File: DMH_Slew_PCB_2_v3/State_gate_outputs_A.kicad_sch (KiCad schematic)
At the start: 26 parts, among them J4 TS_Jack_6.35mm_Sw, J5 TS_Jack_6.35mm_Sw, J51 Conn_01x08_PinHeader, Q5 BC548, Q6 BC548, U1 TL074

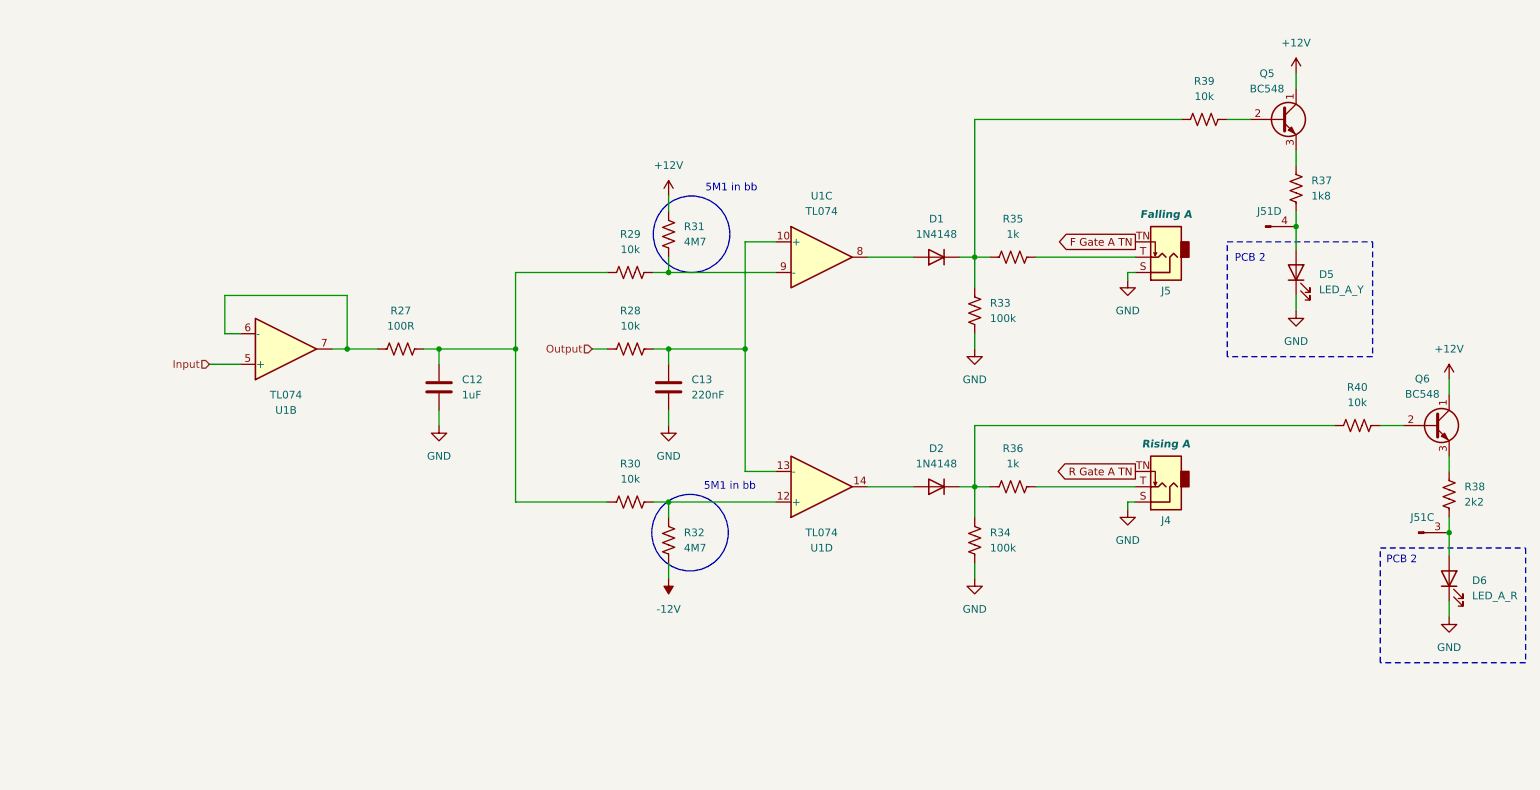
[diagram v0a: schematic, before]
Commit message: Relinked PCB1 and 2 with new v3 schematics
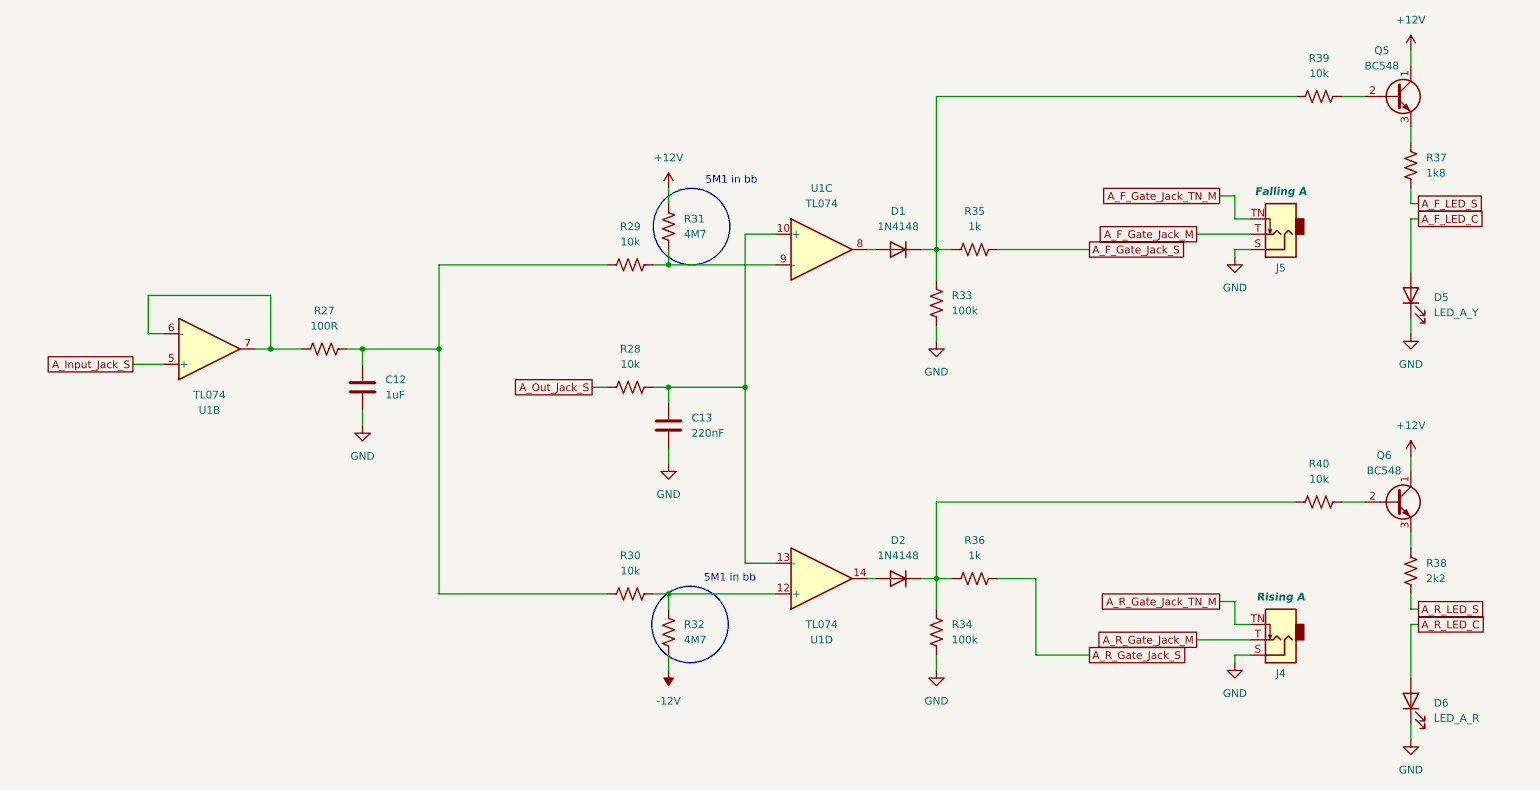
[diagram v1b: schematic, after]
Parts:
- removed J51: Conn_01x08_PinHeader, Connector_PinSocket_2.54mm:PinSocket_1x08_P2.54mm_Vertical, symbol SynthStuff:Conn_01x08_PinHeader
- Q5: footprint Package_TO_SOT_THT:TO-92L_Inline_Wide -> Package_TO_SOT_THT:TO-92_Inline
- U1: footprint Package_DIP:DIP-16_W7.62mm_Socket -> Package_DIP:DIP-14_W7.62mm_Socket
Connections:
- net A_R_LED_C: now reaches D6.2 (A)
- net A_R_LED_C: no longer R38.2
- net A_F_Gate_Jack_M: now reaches J5.T
- net A_F_Gate_Jack_M: no longer R35.1
- net A_F_LED_C: now reaches D5.2 (A)
- net A_F_LED_C: no longer R37.2
- net A_R_Gate_Jack_M: now reaches J4.T
- net A_R_Gate_Jack_M: no longer R36.1
- net F Gate A TN renamed A_F_Gate_Jack_TN_M
- net Input renamed A_Input_Jack_S
- net Output renamed A_Out_Jack_S
- net R Gate A TN renamed A_R_Gate_Jack_TN_M
- new net A_F_Gate_Jack_S: R35.1
- new net A_F_LED_S: R37.2
- new net A_R_Gate_Jack_S: R36.1
- new net A_R_LED_S: R38.2
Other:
- note removed: "PCB 2"
- moved on the sheet: C12, C13, D1, D2, D5, D6, J4, J5, Q5, Q6, R27, R28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

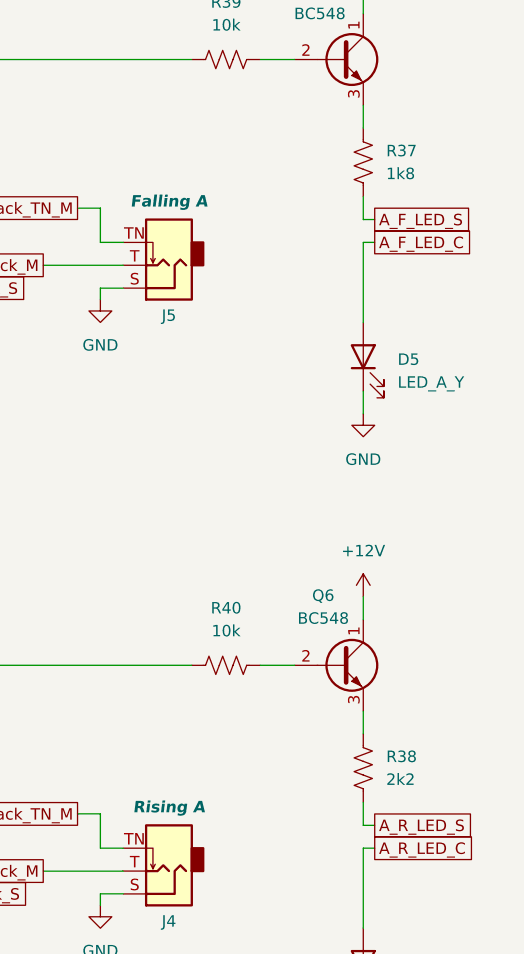
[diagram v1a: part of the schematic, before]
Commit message: Corrected PCB 2 switch positions
and Regenerated Gerbers
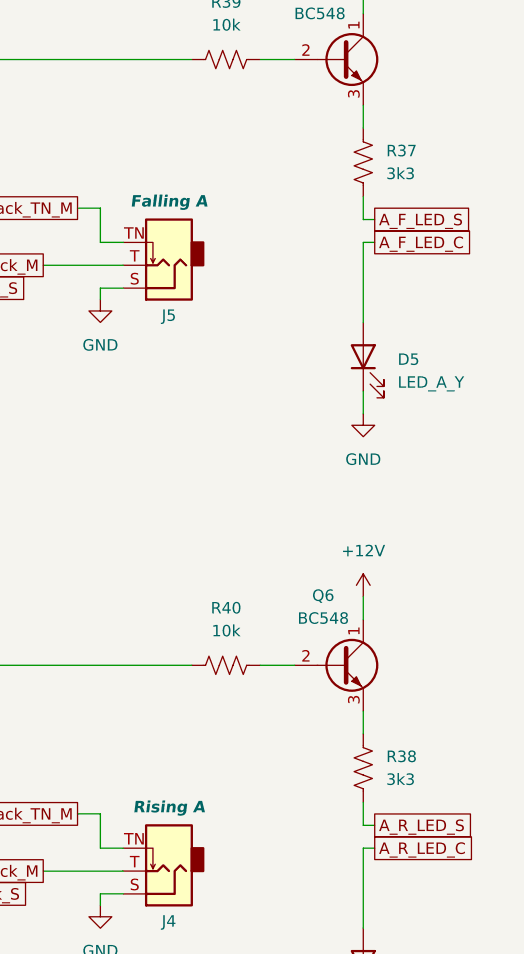
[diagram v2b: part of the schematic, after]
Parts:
- R37: value 1k8 -> 3k3
- R38: value 2k2 -> 3k3
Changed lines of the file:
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@@
 			)
 		)
-		(property "Value" "2k2"
+		(property "Value" "3k3"
 			(at 252.73 114.2999 0)
 			(effects
@@
 			)
 		)
-		(property "Value" "1k8"
+		(property "Value" "3k3"
 			(at 252.73 46.9899 0)
 			(effects

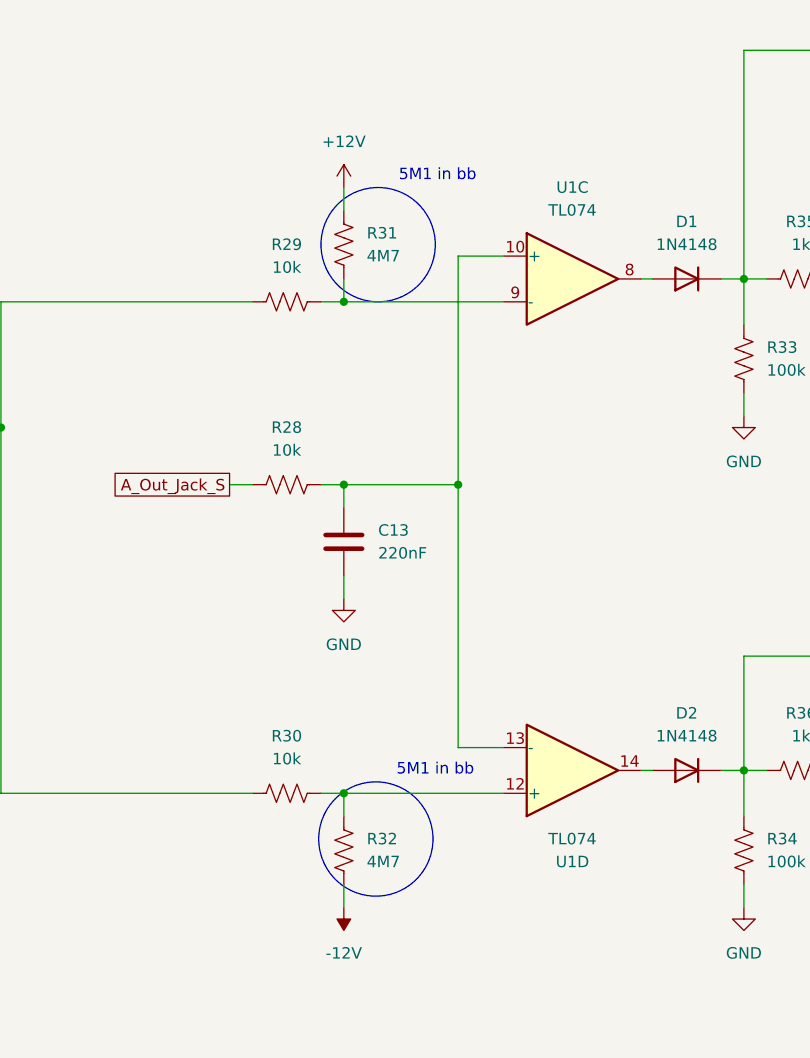
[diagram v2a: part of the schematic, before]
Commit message: Redesigned Main PCB
and regenerated Gerbers
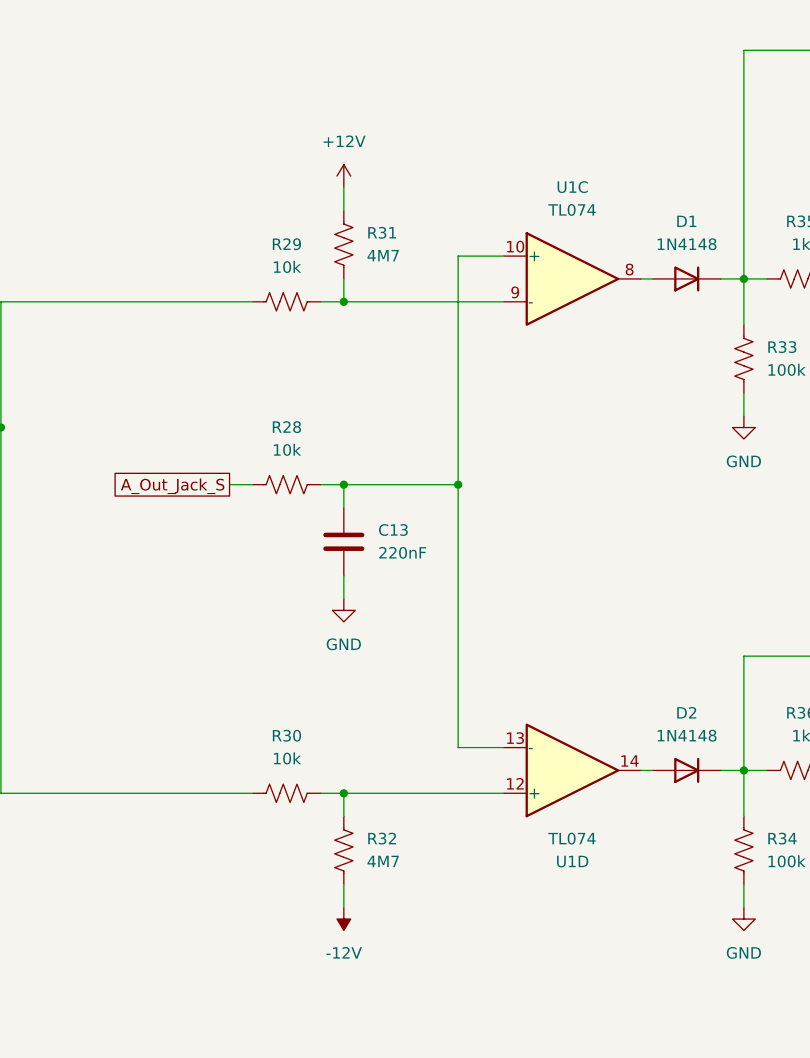
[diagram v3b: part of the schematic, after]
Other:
- note removed: "5M1 in bb"
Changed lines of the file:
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@@
 		(comment 1 "PCB for 5 cm Kosmo format synthesizer module")
-	)
-	(circle
-		(center 130.556 121.92)
-		(radius 6.35)
-		(stroke
-			(width 0)
-			(type default)
-		)
-		(fill
-			(type none)
-		)
-	)
-	(circle
-		(center 130.81 55.88)
-		(radius 6.35)
-		(stroke
-			(width 0)
-			(type default)
-		)
-		(fill
-			(type none)
-		)
-	)
-	(text "5M1 in bb"
-		(exclude_from_sim no)
-		(at 137.16 114.3 0)
-		(effects
-			(font
-				(size 1.27 1.27)
-			)
-		)
-	)
-	(text "5M1 in bb"
-		(exclude_from_sim no)
-		(at 137.414 48.26 0)
-		(effects
-			(font
-				(size 1.27 1.27)
-			)
-		)
 	)
 	(junction
